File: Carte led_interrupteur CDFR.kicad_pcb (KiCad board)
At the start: 2 copper layers, 16 parts, among them J1 Conn_01x10_Female, SW1 SW_Push, SW2 SW_Push, SW3 SW_DIP_x02

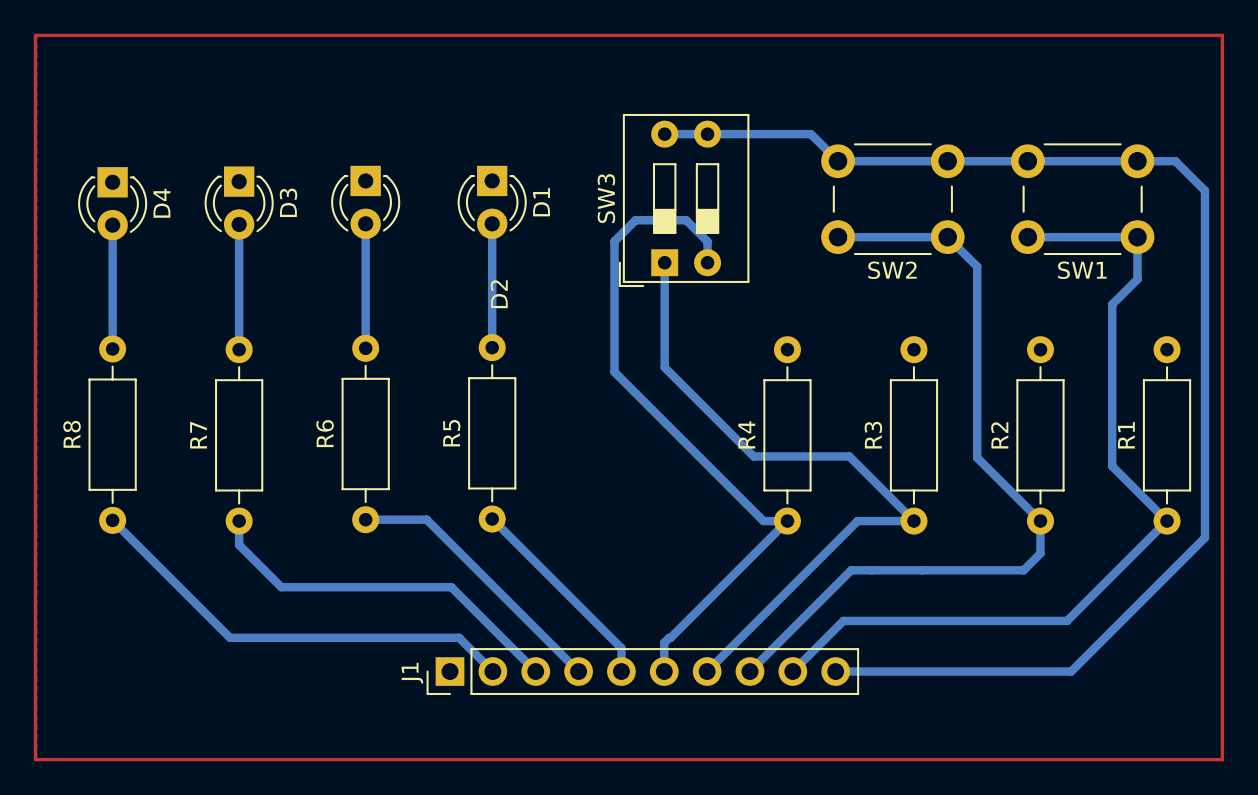
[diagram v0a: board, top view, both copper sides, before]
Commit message: change pin header
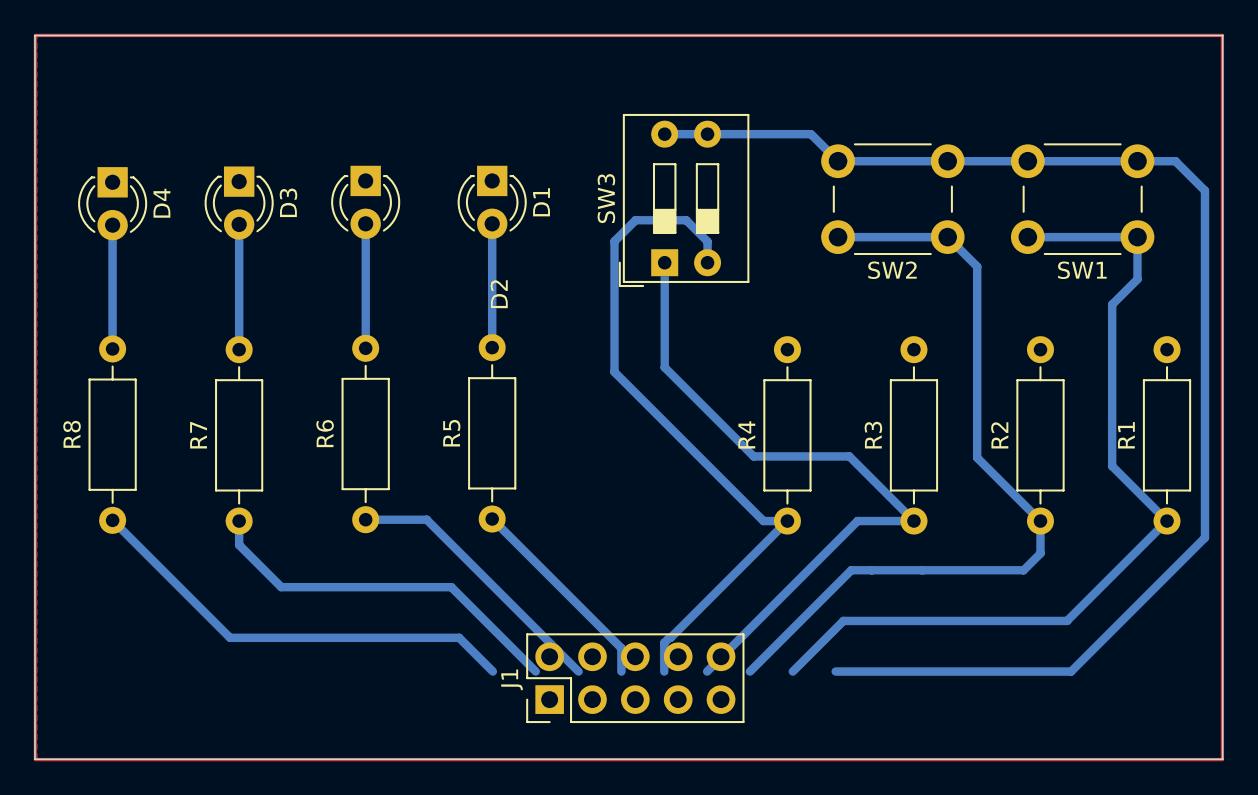
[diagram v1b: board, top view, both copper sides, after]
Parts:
- J1: footprint Connector_PinHeader_2.54mm:PinHeader_1x10_P2.54mm_Vertical -> Connector_PinHeader_2.54mm:PinHeader_2x05_P2.54mm_Vertical
- moved J1 6.13 mm to (120.9, 105.7)
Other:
- board outline added: 70.4 x 42.9 mm
